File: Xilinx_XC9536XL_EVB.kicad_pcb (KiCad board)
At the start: 2 copper layers, 100 x 66 mm, 58 parts, among them IC1 ATTINY2313-P, P1 CONN_7X2, P2 CONN_2, P3 CONN_3X2, P4 CONN_5, P5 CONN_5, P6 CONN_12, P7 CONN_6, P8 CONN_8, SW1 SW_PUSH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

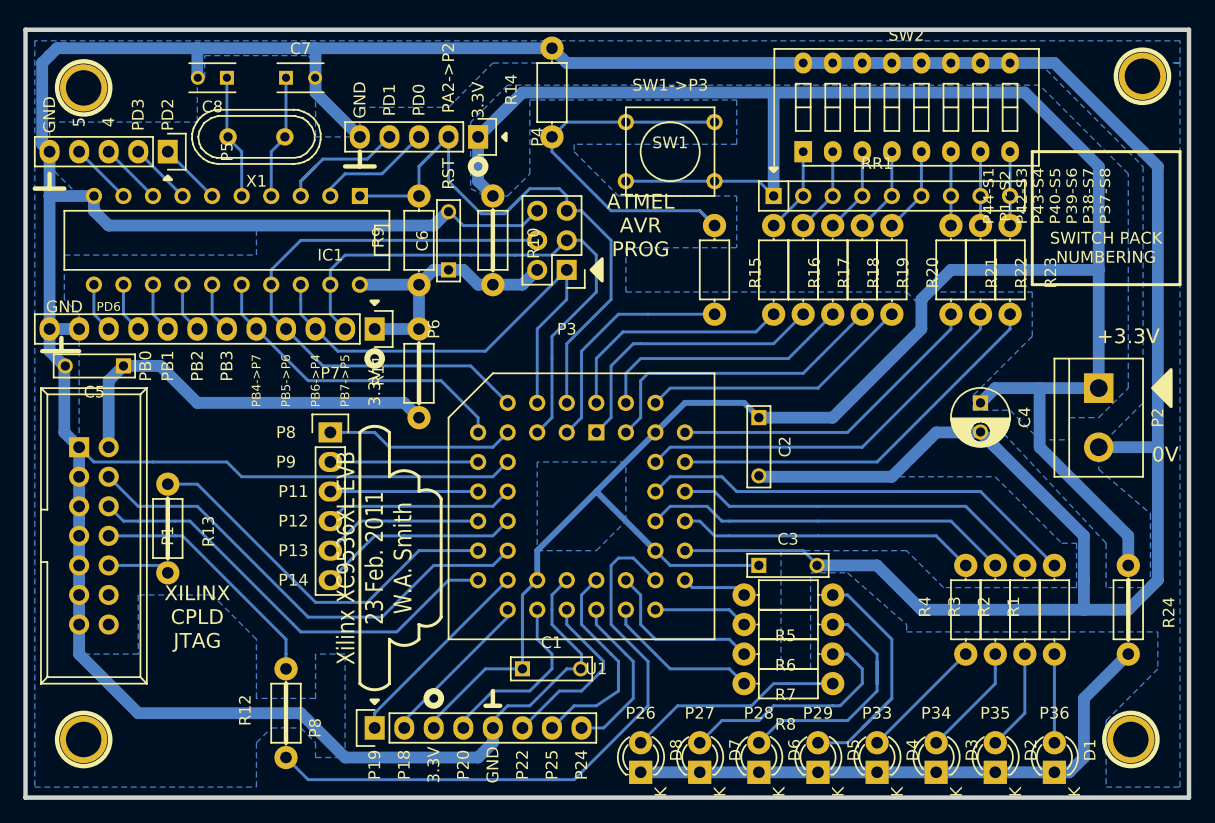
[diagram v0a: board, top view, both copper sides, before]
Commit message: added 3.3v linear regulator
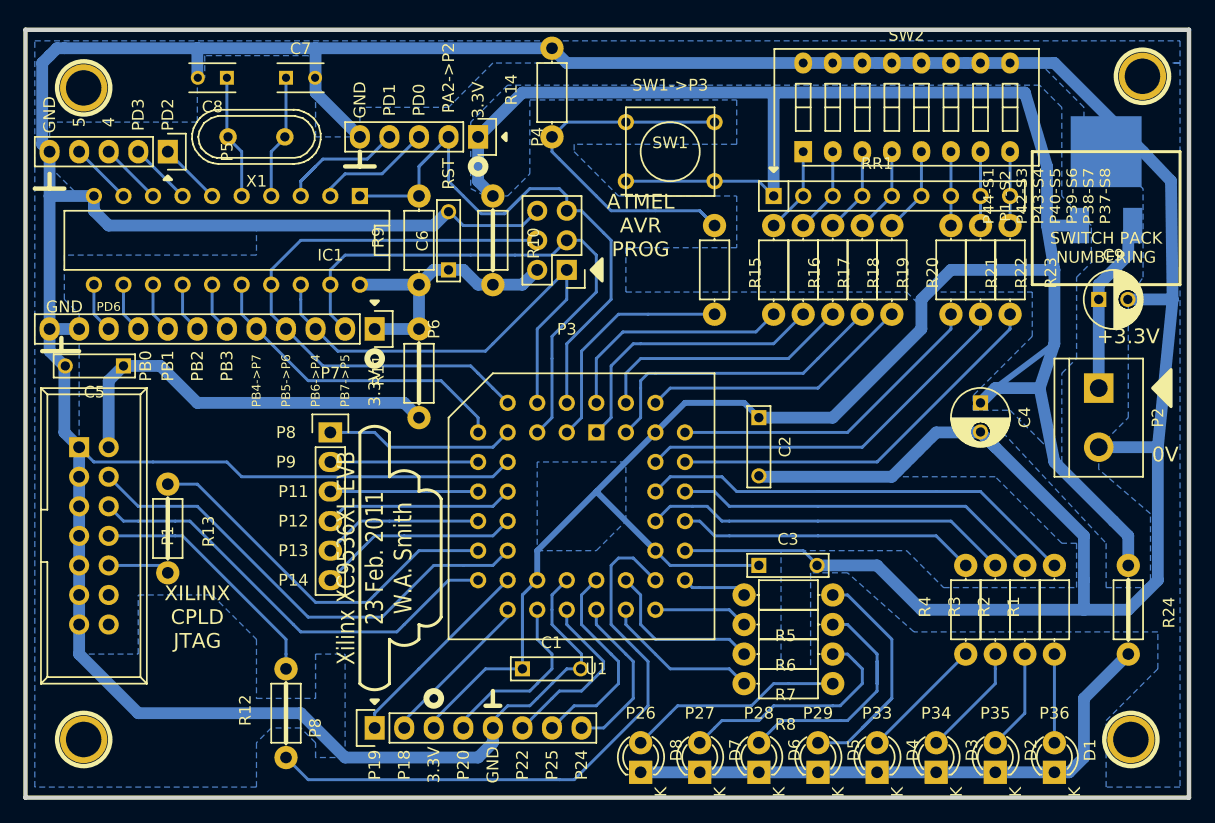
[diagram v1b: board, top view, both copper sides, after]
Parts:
- added C9: 10uF, Capacitors_ThroughHole:C_Radial_D5_L6_P2.5, F.Cu at (142.2, 43.2)
- added U2: SPX2920T-3.3, TO_SOT_Packages_SMD:TO-252-2Lead, B.Cu at (142.9, 36.8)
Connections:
- C1 pad 1: +3.3V -> +3V3
- C2 pad 1: +3.3V -> +3V3
- C3 pad 1: +3.3V -> +3V3
- C4 pad 1: +3.3V -> +3V3
- P2 pad 1: +3.3V -> VCC
- P4 pad 1: +3.3V -> +3V3
- P8 pad 3: +3.3V -> +3V3
- R10 pad 1: +3.3V -> +3V3
- R24 pad 1: +3.3V -> +3V3
- RR1 pad 1: +3.3V -> +3V3
- SW1 pad 2: +3.3V -> +3V3
- U1 pad 21: +3.3V -> +3V3
- U1 pad 32: +3.3V -> +3V3
- U1 pad 41: +3.3V -> +3V3
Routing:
- net +3.3V: track 342.1 -> 0.00 mm
- net +3V3: track 0.00 -> 325.9 mm
- net VCC: track 0.00 -> 16.3 mm
- net GND: track 522.0 -> 526.3 mm
- added copper zone on B.Cu, net +3V3
- removed copper zone on B.Cu, net +3.3V

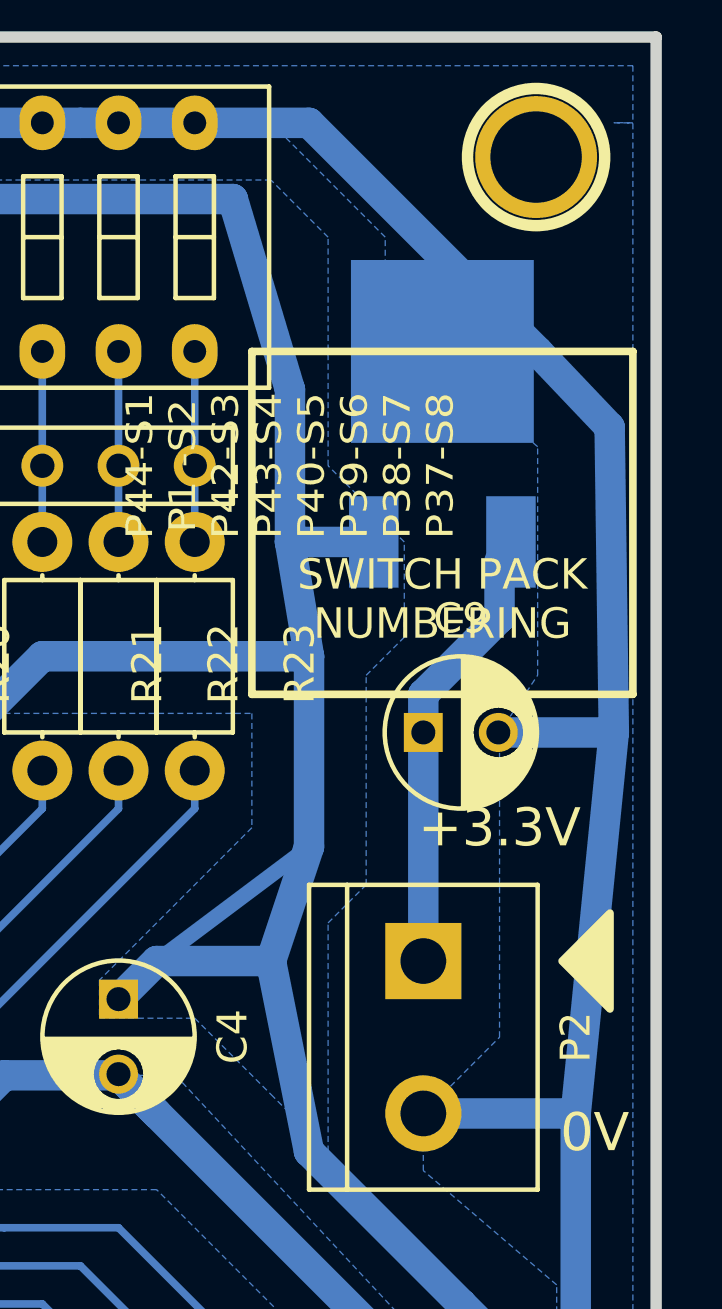
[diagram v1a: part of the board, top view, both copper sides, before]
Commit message: added some space between linear regulator and mounting screw
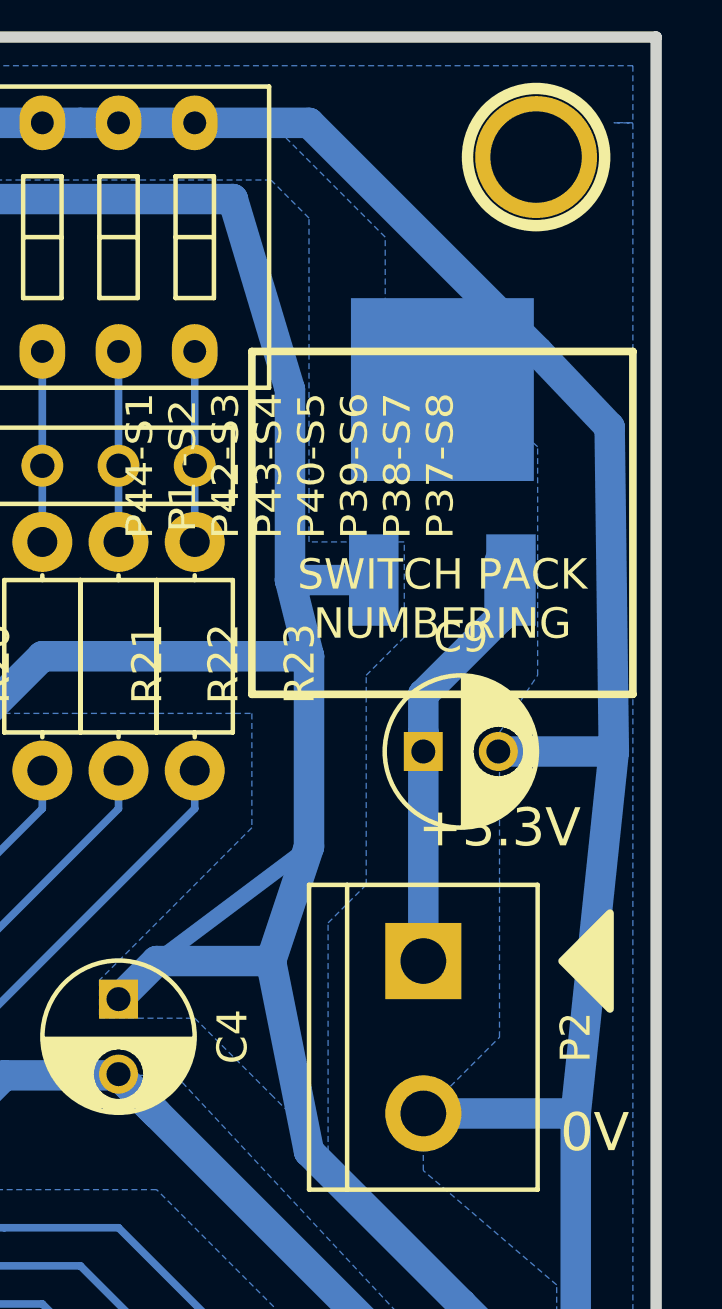
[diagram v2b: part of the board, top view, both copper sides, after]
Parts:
- moved U2 1.27 mm to (142.9, 38.1)
- moved C9 0.63 mm to (142.2, 43.8)
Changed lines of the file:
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@@
   (general
     (links 160)
-    (no_connects 0)
+    (no_connects 1)
     (area 48.208 19.301 150.190201 86.189821)
     (thickness 1.6002)
@@
   )
   (setup
-    (last_trace_width 1.016)
+    (last_trace_width 0.2032)
     (user_trace_width 0.254)
     (user_trace_width 0.508)
@@
   )
   (module Capacitors_ThroughHole:C_Radial_D5_L6_P2.5 (layer Front)
-    (at 142.24 43.18)
+    (at 142.24 43.815)
     (descr "Radial Electrolytic Capacitor Diameter 5mm x Length 6mm, Pitch 2.5mm")
     (tags "Electrolytic Capacitor")
@@
   )
   (module TO_SOT_Packages_SMD:TO-252-2Lead (layer Back)
-    (at 142.875 36.83 180)
+    (at 142.875 38.1 180)
     (descr "DPAK / TO-252 2-lead smd package")
     (tags "dpak TO-252")
@@
   (segment (start 63.5 60.96) (end 62.23 60.96) (width 0.254) (layer Back) (net 32))
   (segment (start 64.77 60.96) (end 63.5 60.96) (width 0.254) (layer Back) (net 32))
-  (segment (start 148.59 43.18) (end 144.74 43.18) (width 1.016) (layer Back) (net 33))
+  (segment (start 148.59 43.815) (end 144.78 43.815) (width 1.016) (layer Back) (net 33))
   (segment (start 90.17 81.28) (end 88.9 82.55) (width 0.254) (layer Back) (net 33))
   (segment (start 88.9 82.55) (end 77.47 82.55) (width 0.254) (layer Back) (net 33))
@@
   (segment (start 147.32 67.31) (end 147.32 55.88) (width 1.016) (layer Back) (net 33))
   (segment (start 127 69.85) (end 123.19 66.04) (width 1.016) (layer Back) (net 33))
-  (segment (start 147.32 55.88) (end 148.59 43.18) (width 1.016) (layer Back) (net 33))
-  (segment (start 148.59 43.18) (end 148.45061 33.004512) (width 1.016) (layer Back) (net 33))
+  (segment (start 147.32 55.88) (end 148.59 43.815) (width 1.016) (layer Back) (net 33))
+  (segment (start 148.59 43.815) (end 148.45061 33.004512) (width 1.016) (layer Back) (net 33))
   (segment (start 146.05 30.48) (end 138.43 22.86) (width 1.016) (layer Back) (net 33))
   (segment (start 138.43 22.86) (end 130.81 22.86) (width 1.016) (layer Back) (net 33))
@@
   (segment (start 134.62 36.83) (end 134.62 34.29) (width 0.254) (layer Back) (net 76) (status C00))
   (segment (start 134.62 34.29) (end 134.62 30.48) (width 0.254) (layer Back) (net 76) (status C00))
-  (segment (start 137.795 36.83) (end 140.335 36.83) (width 1.016) (layer Back) (net 77))
+  (segment (start 137.795 38.1) (end 140.335 38.1) (width 1.016) (layer Back) (net 77))
   (segment (start 138.43 46.99) (end 133.35 50.8) (width 0.254) (layer Back) (net 77) (status 800))
   (segment (start 101.6 33.02) (end 109.22 33.02) (width 0.254) (layer Back) (net 77) (status C00))
@@
   (segment (start 135.89 25.4) (end 114.3 25.4) (width 1.016) (layer Back) (net 77))
   (segment (start 137.795 31.75) (end 135.89 25.4) (width 1.016) (layer Back) (net 77))
-  (segment (start 138.43 40.64) (end 137.795 36.83) (width 1.016) (layer Back) (net 77))
-  (segment (start 137.795 36.83) (end 137.795 31.75) (width 1.016) (layer Back) (net 77))
+  (segment (start 138.43 40.64) (end 137.795 38.1) (width 1.016) (layer Back) (net 77))
+  (segment (start 137.795 38.1) (end 137.795 31.75) (width 1.016) (layer Back) (net 77))
   (segment (start 138.43 46.99) (end 138.43 40.64) (width 1.016) (layer Back) (net 77) (status 800))
   (segment (start 119.38 53.34) (end 113.03 53.34) (width 1.016) (layer Back) (net 77) (status 400))
@@
       (pts
         (xy 139.065 57.15) (xy 139.065 49.53) (xy 140.335 48.26) (xy 140.335 41.275) (xy 141.605 40.005)
-        (xy 141.605 36.83) (xy 139.065 34.29) (xy 139.065 26.67) (xy 137.16 24.765) (xy 91.44 24.765)
+        (xy 141.605 36.83) (xy 138.43 36.83) (xy 138.43 26.035) (xy 137.16 24.765) (xy 91.44 24.765)
         (xy 88.265 27.94) (xy 88.265 33.655) (xy 89.535 34.29) (xy 91.44 34.29) (xy 93.345 32.385)
         (xy 93.345 26.035) (xy 111.125 26.035) (xy 111.125 29.845) (xy 97.155 29.845) (xy 97.155 30.48)
